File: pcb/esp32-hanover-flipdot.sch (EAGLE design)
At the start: 28 parts, among them J1 DC-005, J2 HANOVER, J3 FTDI, Q1 NCE3407A, Q2 S9013, U1 ESP32-PICO-D4, U2 CJA1117B-3.3-SOT89, U3 LM2576S

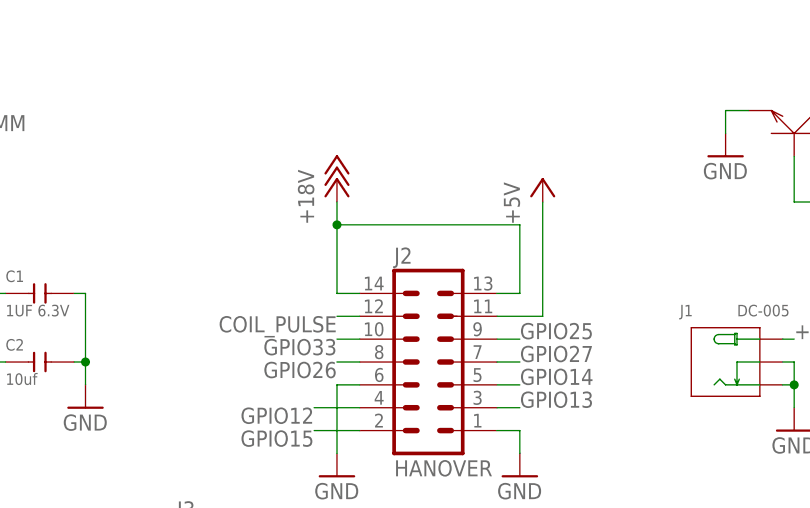
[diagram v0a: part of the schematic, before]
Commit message: PCB: Disconnect dot board pin 13, 14. Add 18VDC and warning text. Increase space around J2.
Disconnect dot-board pin 13 and 14 from 18VDC, seems to cause overheating of dot 0,0 on dot boards when boards are not enabled. Works fine without anyway - tested by cutting ribbon cable pins 13, 14.

Added 18VDC only warning text. Add warning text to disconnect power before connecting or disconnecting dot boards.

Increase space around J2 as the connector housing is causing stress to neighboring components.
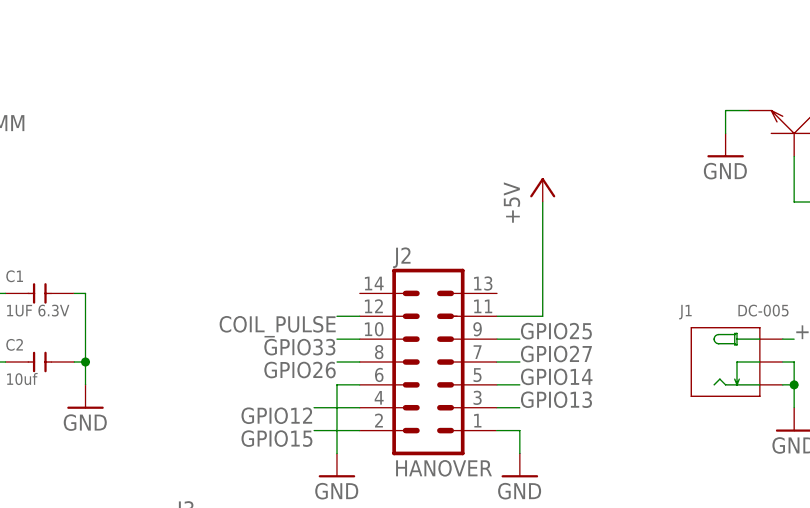
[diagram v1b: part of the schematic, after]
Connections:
- net +18V: no longer J2.13, J2.14

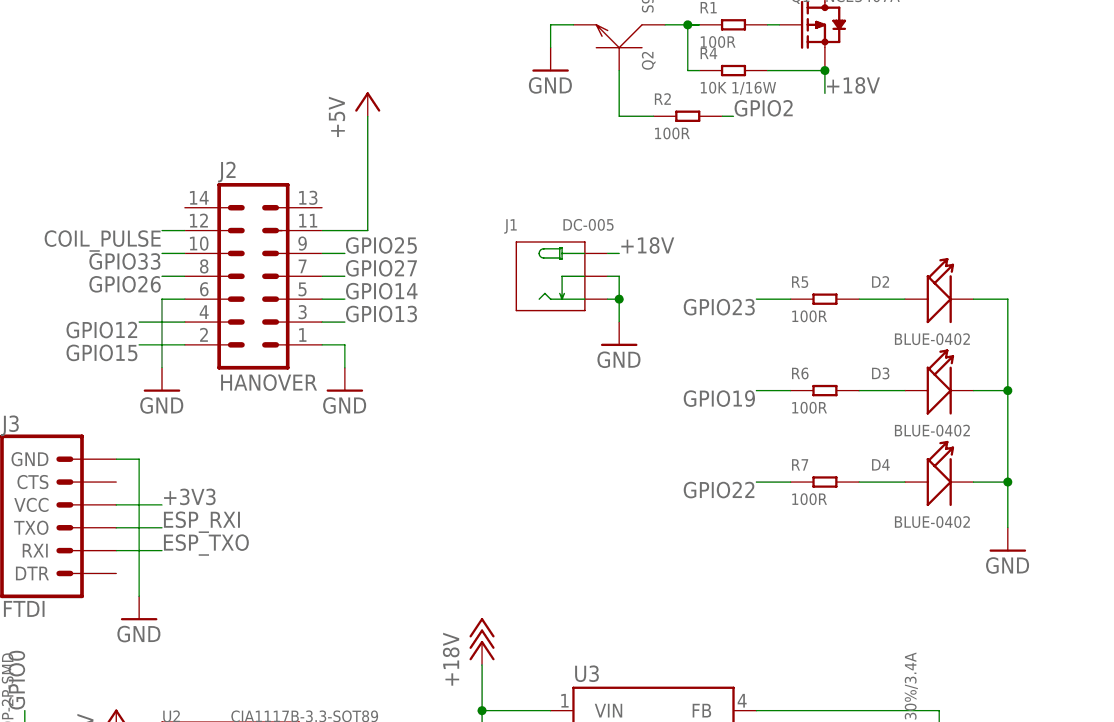
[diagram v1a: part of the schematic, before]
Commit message: PCB: Layout improvements and parts substitutions
Board:
* Increase ground plane stitching especially for heatsinking of regulators and ESP32
* Add pour and stitching on +3V3 LDO regulator for heatsinking
* Increase voltage trace sizes to conduct heat away from power components/decrease voltage droop

Schematic:
* Disconnect dot board pin 14 from 18V, it seems to cause erratic behavior on dot boards. Not sure what the function of this 18V supply pin is, but boards work fine with this line snipped off
* Add dot board pin 13 to existing COIL_PULSE net on pin 14, as they are internally shorted on the dot boards - this should double the current capacity/halve the voltage droop on the cable to the first dot board
* Parts swapped with latest Eagle online libraries where applicable

Schematic/BoM:
* D2, D3, D4: Swap from blue LEDs to white LEDs
* R5, R6, R7: Swap from 100R to 150R (LED current limiting resistors)
* RST, PGM: Swap to substitute part with same dimensions on Seeed OPL as original part no longer available
* U3: Swap BoM MPN to LM2576SX-5.0/NOPB as it has ready pricing on Seeed Fusion PCBA

Library:
* Add custom library for Seeed 5.5/2.1 DC jack without polarity silkscreen, use it on board

Misc:
* Generate latest Gerbers for Seeed Fusion PCB 2 layer
* Update board image
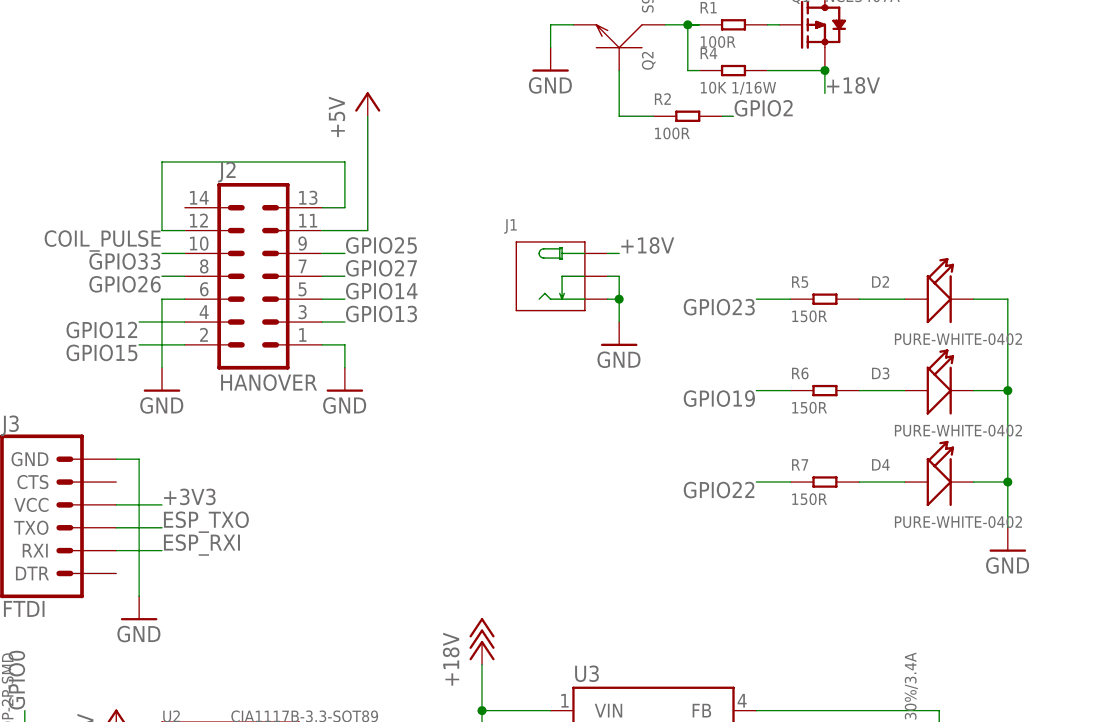
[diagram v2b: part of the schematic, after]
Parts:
- C1: device Seeed-Capacitor:CERAMIC-1UF-6.3V-10%-X5R(0402) -> OPL_Capacitor:CERAMIC-1UF-6.3V-10%-X5R(0402)
- C2: device Seeed-Capacitor:CERAMIC-10UF-6.3V-20%-X5R(0402) -> OPL_Capacitor:CERAMIC-10UF-6.3V-20%-X5R(0402)
- C3: device Seeed-Capacitor:CERAMIC-100NF-25V-10%-X7R(0402) -> OPL_Capacitor:CERAMIC-100NF-25V-10%-X7R(0402)
- CT1: device Seeed-Capacitor:ALUMINUM-SMD-220UF-16V(D6.3-H7.7MM) -> OPL_Capacitor:ALUMINUM-SMD-220UF-16V(D6.3-H7.7MM); MPN (none) -> 302030000
- CT2: device Seeed-Capacitor:ALUMINUM-SMD-220UF-16V(D6.3-H7.7MM) -> OPL_Capacitor:ALUMINUM-SMD-220UF-16V(D6.3-H7.7MM)
- D1: device Seeed-Diode:SMD-DIODE-SCHOTTKY-28V-5A(DO-214AA) -> OPL_Discrete_Semiconductor:SMD-DIODE-SCHOTTKY-28V-5A(DO-214AA)
- D2, D3, D4: value BLUE-0402 -> PURE-WHITE-0402; device Seeed-LED:SMD-LED-CLEAR-BLUE(0402) -> OPL_Optoelectronics:SMD-LED-YELLOW-DIFFUSED-PURE-WHITE(0402)
- J1: device Seeed-Connector:CONN-POWER-JACK-2.1MM(DC-005) -> OPL_Connector_DC-005_No_Polarity_Markings:JACK-DC-005'DC-005'
- PGM, RST: device Seeed-Switch:SMD-BUTTON(2P-3.0X2.5X1.2+0.4MM)-B3U-1000P-2P-SMD -> OPL_Switch:SMD-BUTTON(2P-3.0X2.5X1.2+0.4MM)-B3U-1000P-2P-SMD
- Q1: device Seeed-Transistor:SMD-MOSFET-P-CH-VDC=30V-ID=4.3A-NCE3407A(SOT-23) -> OPL_Discrete_Semiconductor:SMD-MOSFET-P-CH-VDC=30V-ID=4.3A-NCE3407A(SOT-23)
- Q2: device Seeed-Transistor:SMD-TRANSISTORS-NPN-25V-500MA-S9013(SOT-23) -> OPL_Discrete_Semiconductor:SMD-TRANSISTORS-NPN-25V-500MA-S9013(SOT-23)
- R1, R2: device Seeed-Resistor:SMD-RES-100R-5%-1/16W(0402) -> OPL_Resistor:SMD-RES-100R-5%-1/16W(0402)
- R3, R4: device Seeed-Resistor:SMD-RES-10K-1%-1/16W(0402) -> OPL_Resistor:SMD-RES-10K-1%-1/16W(0402)
- R5, R6, R7: value 100R -> 150R; device Seeed-Resistor:SMD-RES-100R-5%-1/16W(0402) -> OPL_Resistor:SMD-RES-150R-1%-1/16W(0402); MPN (none) -> RC0402FR-07150RL
- U2: device Seeed-IC:PMIC-CJA1117B-3.3(SOT-89) -> OPL_IC:PMIC-CJA1117B-3.3(SOT-89)
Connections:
- net COIL_PULSE: now also J2.13
- net ESP_RXI: now also J3.RXI; no longer J3.TXO
- net ESP_TXO: now also J3.TXO; no longer J3.RXI

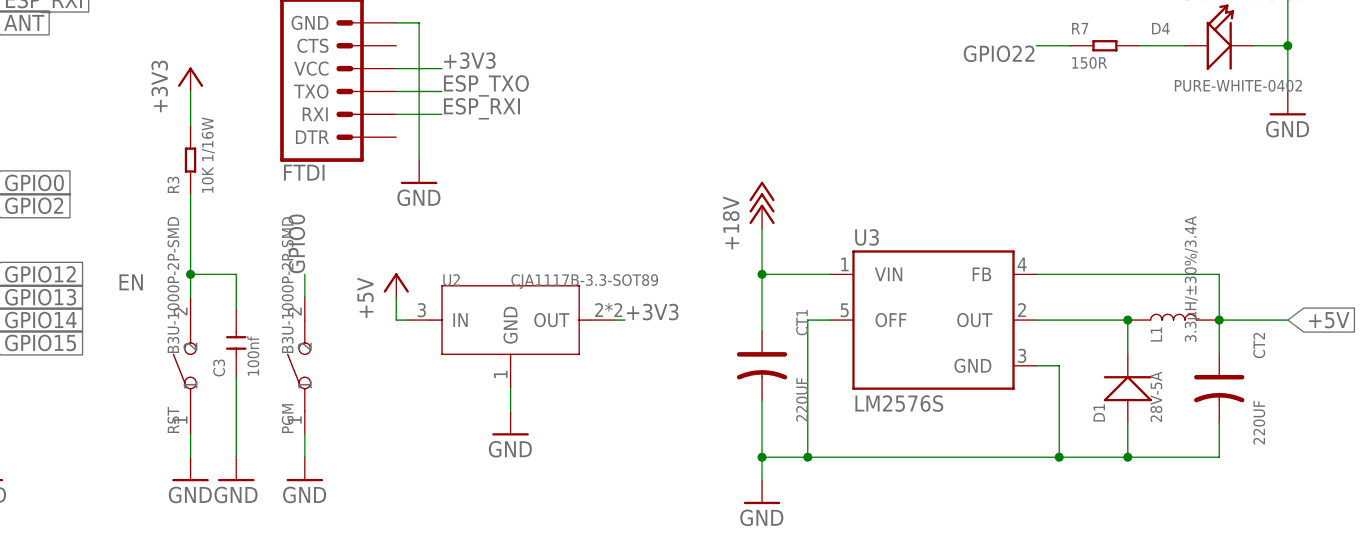
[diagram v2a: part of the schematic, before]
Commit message: PCB: Cleanup for Seeed Fusion
Board and Schematic:
* Change LM2576 part to match BOM

Other documents:
* Exported a new set of Gerbers and matching pick and place files and top of PCB drawing
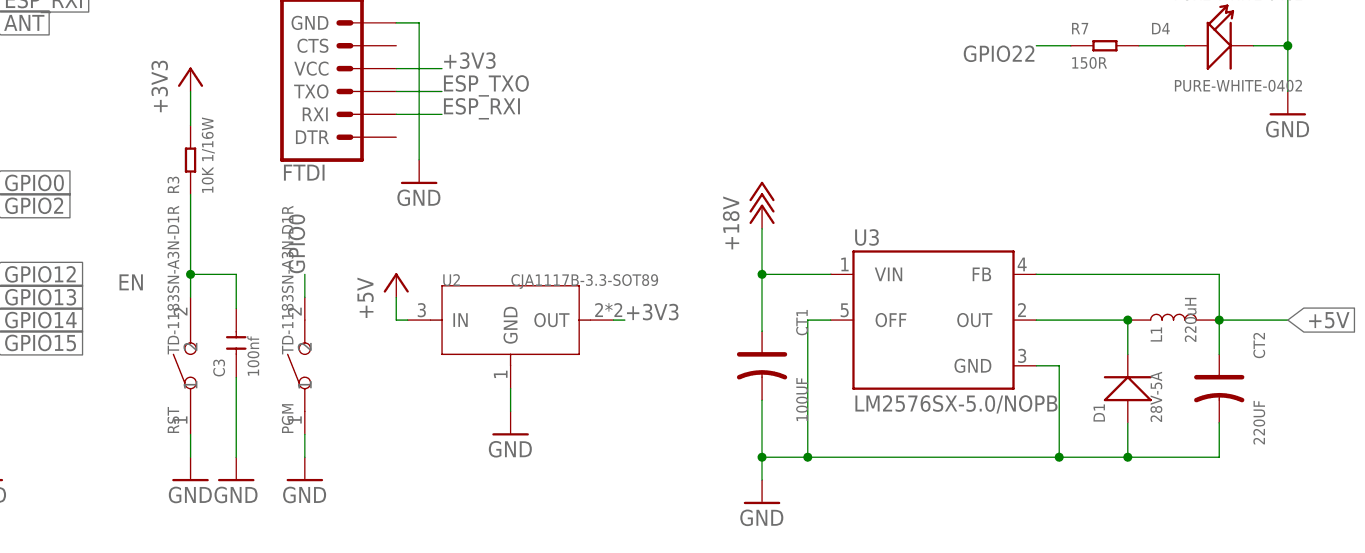
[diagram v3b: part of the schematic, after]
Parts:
- CT1: value 220UF -> 100UF
- L1: value 3.3µH/±30%/3.4A -> 220uH
- PGM, RST: value B3U-1000P-2P-SMD -> TD-1183SN-A3N-D1R
- U3: value LM2576S -> LM2576SX-5.0/NOPB
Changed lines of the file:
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@@
 <part name="GND3" library="supply1" library_urn="urn:adsk.eagle:library:371" deviceset="GND" device=""/>
 <part name="E1" library="SparkFun-RF" library_urn="urn:adsk.eagle:library:531" deviceset="ANTENNA-GROUNDED" device="TRACE-15.2MM" package3d_urn="urn:adsk.eagle:package:39575/1"/>
-<part name="RST" library="OPL_Switch" library_urn="urn:adsk.eagle:library:8004989" deviceset="SMD-BUTTON(2P-3.0X2.5X1.2+0.4MM)" device="-B3U-1000P-2P-SMD" package3d_urn="urn:adsk.eagle:package:8005100/1" value="B3U-1000P-2P-SMD"/>
+<part name="RST" library="OPL_Switch" library_urn="urn:adsk.eagle:library:8004989" deviceset="SMD-BUTTON(2P-3.0X2.5X1.2+0.4MM)" device="-B3U-1000P-2P-SMD" package3d_urn="urn:adsk.eagle:package:8005100/1" value="TD-1183SN-A3N-D1R"/>
 <part name="R3" library="OPL_Resistor" library_urn="urn:adsk.eagle:library:8004883" deviceset="SMD-RES-10K-1%-1/16W(0402)" device="" package3d_urn="urn:adsk.eagle:package:8004940/1" value="10K 1/16W"/>
 <part name="+3V3" library="supply1" library_urn="urn:adsk.eagle:library:371" deviceset="+3V3" device=""/>
@@
 <part name="J1" library="OPL_Connector_DC-005_No_Polarity_Markings" deviceset="JACK-DC-005" device="'DC-005'" package3d_urn="urn:adsk.eagle:package:8004569/2" value="DC-005"/>
 <part name="R4" library="OPL_Resistor" library_urn="urn:adsk.eagle:library:8004883" deviceset="SMD-RES-10K-1%-1/16W(0402)" device="" package3d_urn="urn:adsk.eagle:package:8004940/1" value="10K 1/16W"/>
-<part name="PGM" library="OPL_Switch" library_urn="urn:adsk.eagle:library:8004989" deviceset="SMD-BUTTON(2P-3.0X2.5X1.2+0.4MM)" device="-B3U-1000P-2P-SMD" package3d_urn="urn:adsk.eagle:package:8005100/1" value="B3U-1000P-2P-SMD"/>
+<part name="PGM" library="OPL_Switch" library_urn="urn:adsk.eagle:library:8004989" deviceset="SMD-BUTTON(2P-3.0X2.5X1.2+0.4MM)" device="-B3U-1000P-2P-SMD" package3d_urn="urn:adsk.eagle:package:8005100/1" value="TD-1183SN-A3N-D1R"/>
 <part name="GND10" library="supply1" library_urn="urn:adsk.eagle:library:371" deviceset="GND" device=""/>
-<part name="U3" library="LM2576 (1)" deviceset="LM2576" device="S"/>
-<part name="CT1" library="OPL_Capacitor" library_urn="urn:adsk.eagle:library:8004261" deviceset="ALUMINUM-SMD-220UF-16V(D6.3-H7.7MM)" device="" package3d_urn="urn:adsk.eagle:package:8004282/1" value="220UF">
+<part name="U3" library="LM2576 (1)" deviceset="LM2576" device="S" value="LM2576SX-5.0/NOPB"/>
+<part name="CT1" library="OPL_Capacitor" library_urn="urn:adsk.eagle:library:8004261" deviceset="ALUMINUM-SMD-220UF-16V(D6.3-H7.7MM)" device="" package3d_urn="urn:adsk.eagle:package:8004282/1" value="100UF">
 <attribute name="MPN" value="302030000"/>
 </part>
@@
 <part name="D1" library="OPL_Discrete_Semiconductor" library_urn="urn:adsk.eagle:library:8004488" deviceset="SMD-DIODE-SCHOTTKY-28V-5A(DO-214AA)" device="" package3d_urn="urn:adsk.eagle:package:8004541/1" value="28V-5A"/>
 <part name="CT2" library="OPL_Capacitor" library_urn="urn:adsk.eagle:library:8004261" deviceset="ALUMINUM-SMD-220UF-16V(D6.3-H7.7MM)" device="" package3d_urn="urn:adsk.eagle:package:8004282/1" value="220UF"/>
-<part name="L1" library="SparkFun-Coils" library_urn="urn:adsk.eagle:library:512" deviceset="INDUCTOR" device="-CR54-3.3UH" package3d_urn="urn:adsk.eagle:package:37572/1" value="3.3µH/±30%/3.4A"/>
+<part name="L1" library="SparkFun-Coils" library_urn="urn:adsk.eagle:library:512" deviceset="INDUCTOR" device="-CR54-3.3UH" package3d_urn="urn:adsk.eagle:package:37572/1" value="220uH"/>
 <part name="D2" library="OPL_Optoelectronics" library_urn="urn:adsk.eagle:library:8004780" deviceset="SMD-LED-YELLOW-DIFFUSED-PURE-WHITE(0402)" device="" package3d_urn="urn:adsk.eagle:package:8004828/1" value="PURE-WHITE-0402"/>
 <part name="D3" library="OPL_Optoelectronics" library_urn="urn:adsk.eagle:library:8004780" deviceset="SMD-LED-YELLOW-DIFFUSED-PURE-WHITE(0402)" device="" package3d_urn="urn:adsk.eagle:package:8004828/1" value="PURE-WHITE-0402"/>

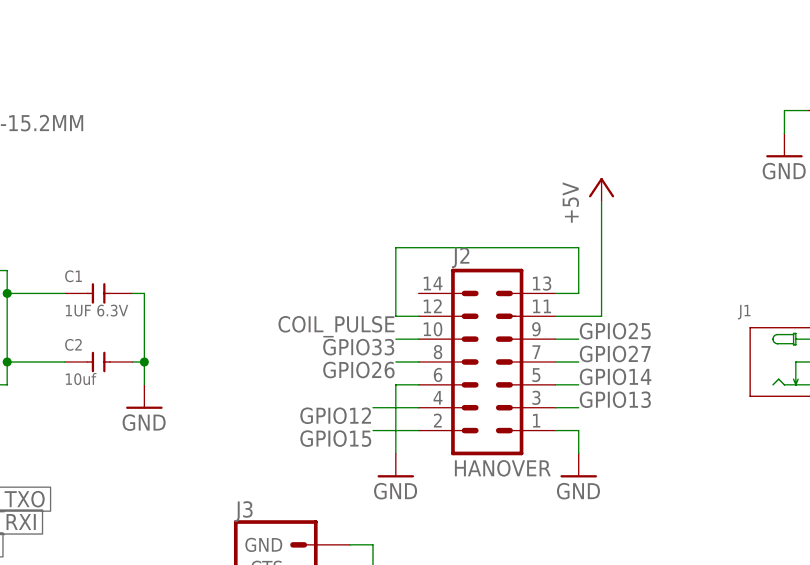
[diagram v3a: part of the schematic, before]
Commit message: pcb: Connect dot board pin 14 to COIL_PULSE (pin 12, pin 13) too
The 18V supply on this pin doesn't seem to be used, as it's wired to column darlington arrays while the dot boards seem to use the row darlingtons to source/sink. In any case, it should be safe to connect, tested splicing pin 12+13+14 together on a real dot board and it worked fine.
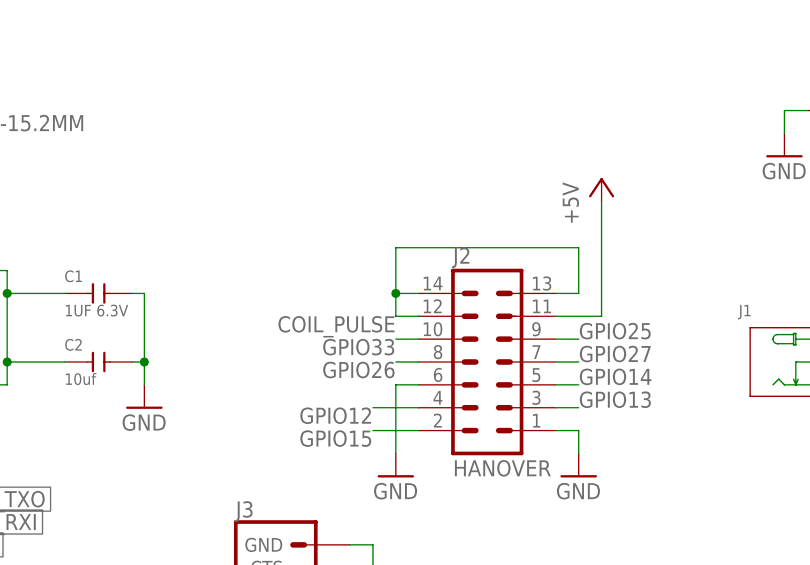
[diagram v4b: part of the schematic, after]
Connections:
- net COIL_PULSE: now also J2.14
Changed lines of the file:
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@@
 <wire x1="127" y1="91.44" x2="127" y2="96.52" width="0.1524" layer="91"/>
 <wire x1="127" y1="96.52" x2="106.68" y2="96.52" width="0.1524" layer="91"/>
-<wire x1="106.68" y1="96.52" x2="106.68" y2="88.9" width="0.1524" layer="91"/>
+<wire x1="106.68" y1="96.52" x2="106.68" y2="91.44" width="0.1524" layer="91"/>
+<pinref part="J2" gate="1" pin="14"/>
+<wire x1="106.68" y1="91.44" x2="106.68" y2="88.9" width="0.1524" layer="91"/>
+<wire x1="106.68" y1="91.44" x2="109.22" y2="91.44" width="0.1524" layer="91"/>
+<junction x="106.68" y="91.44"/>
 </segment>
 <segment>
